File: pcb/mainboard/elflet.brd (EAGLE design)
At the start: 32 x 58 mm, 37 parts, among them J1 ZX62-B-5PA(33), J2 2212S-10SG-36, J3 STD-PINHD-1X6, Q1 IRLML6344TRPBF, Q2 ALS-PT19-315C/L177/TR8, SW1 SKRPACE010, U1 ESP-WROOM-32, U2 ADP3338AKCZ-3.3, U3 OSRB38C9AA, U4 BME280

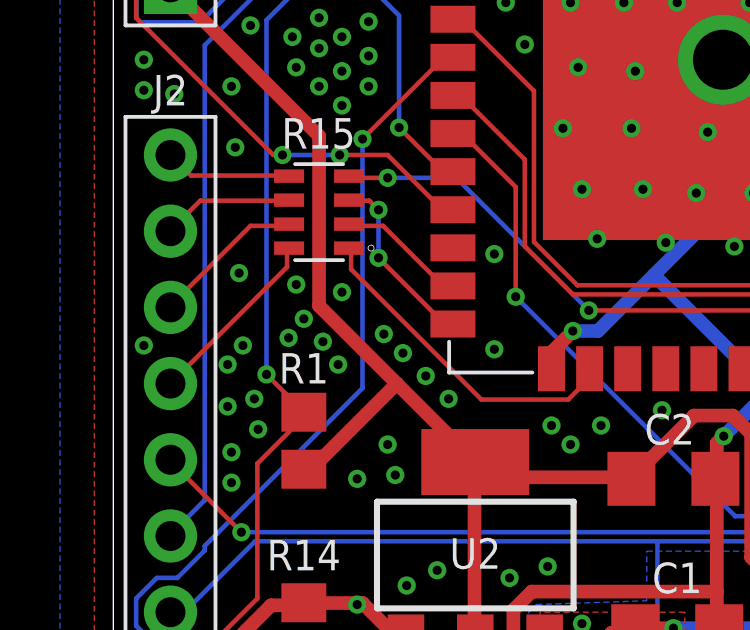
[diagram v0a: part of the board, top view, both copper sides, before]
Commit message: add logo silk
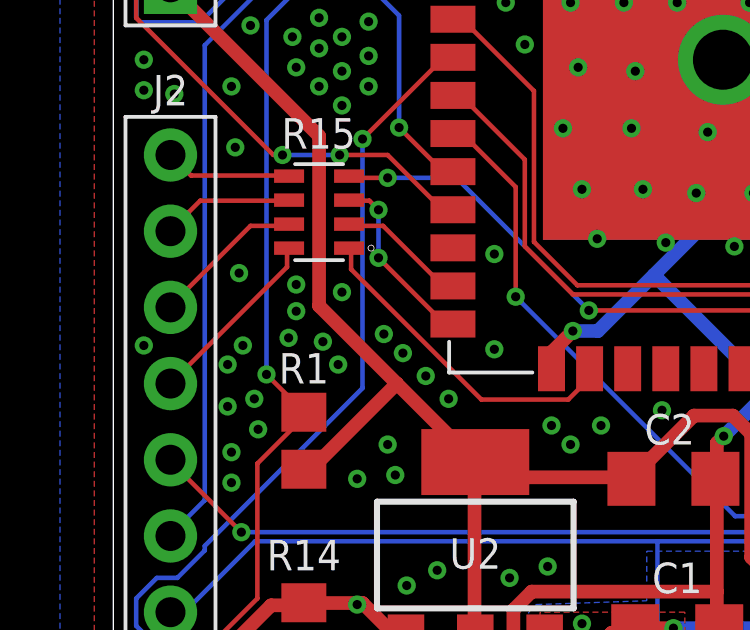
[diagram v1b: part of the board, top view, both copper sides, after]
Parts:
- added U$1: (no value), logo:ELFLET-LOGO
- added U$2: (no value), logo:ELFLET-QRCODE
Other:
- board text added: "ver 1.0"
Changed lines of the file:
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@@
 <dimension x1="0" y1="58" x2="32" y2="58" x3="16" y3="64.77" textsize="1.778" layer="47" visible="yes"/>
 <dimension x1="0" y1="0" x2="0" y2="58" x3="-8.89" y3="29" textsize="1.778" layer="47" visible="yes"/>
+<text x="12.319" y="5.588" size="1.4224" layer="22" font="vector" rot="MR0">ver 1.0</text>
 </plain>
 <attributes>
@@
 <attribute name="VALUE" x="-0.592" y="54.862" size="1.27" layer="27" font="vector" rot="R270" align="center"/>
 </element>
+<element name="U$1" library="logo" package="ELFLET-LOGO" value="" x="26.924" y="7.747" rot="MR0"/>
+<element name="U$2" library="logo" package="ELFLET-QRCODE" value="" x="25.908" y="33.528" rot="MR0"/>
 </elements>
 <signals>
@@
 <via x="7.493" y="17.78" extent="1-16" drill="0.3048"/>
 <via x="6.985" y="18.542" extent="1-16" drill="0.3048"/>
-<via x="6.35" y="19.304" extent="1-16" drill="0.3048"/>
+<via x="6.096" y="19.558" extent="1-16" drill="0.3048"/>
 <via x="6.096" y="20.447" extent="1-16" drill="0.3048"/>
 <via x="5.842" y="18.669" extent="1-16" drill="0.3048"/>

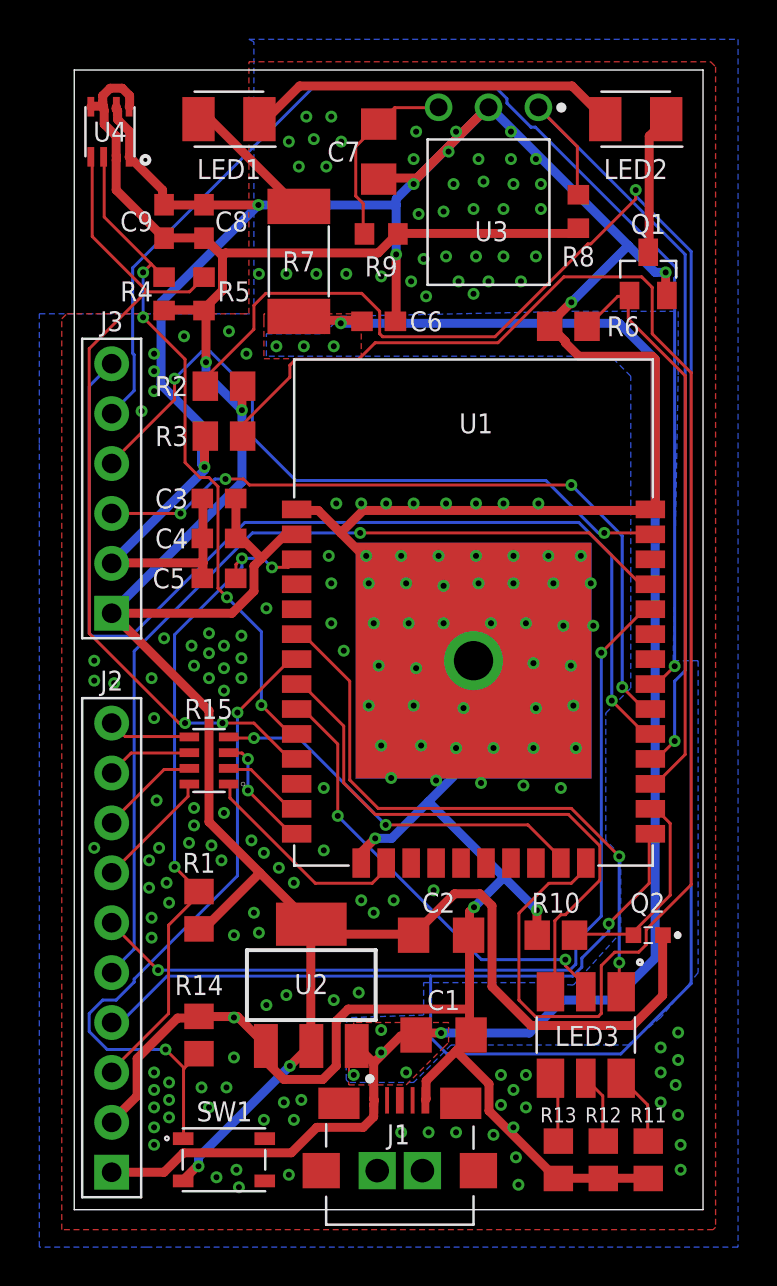
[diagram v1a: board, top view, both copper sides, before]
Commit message: optimized for panerizing
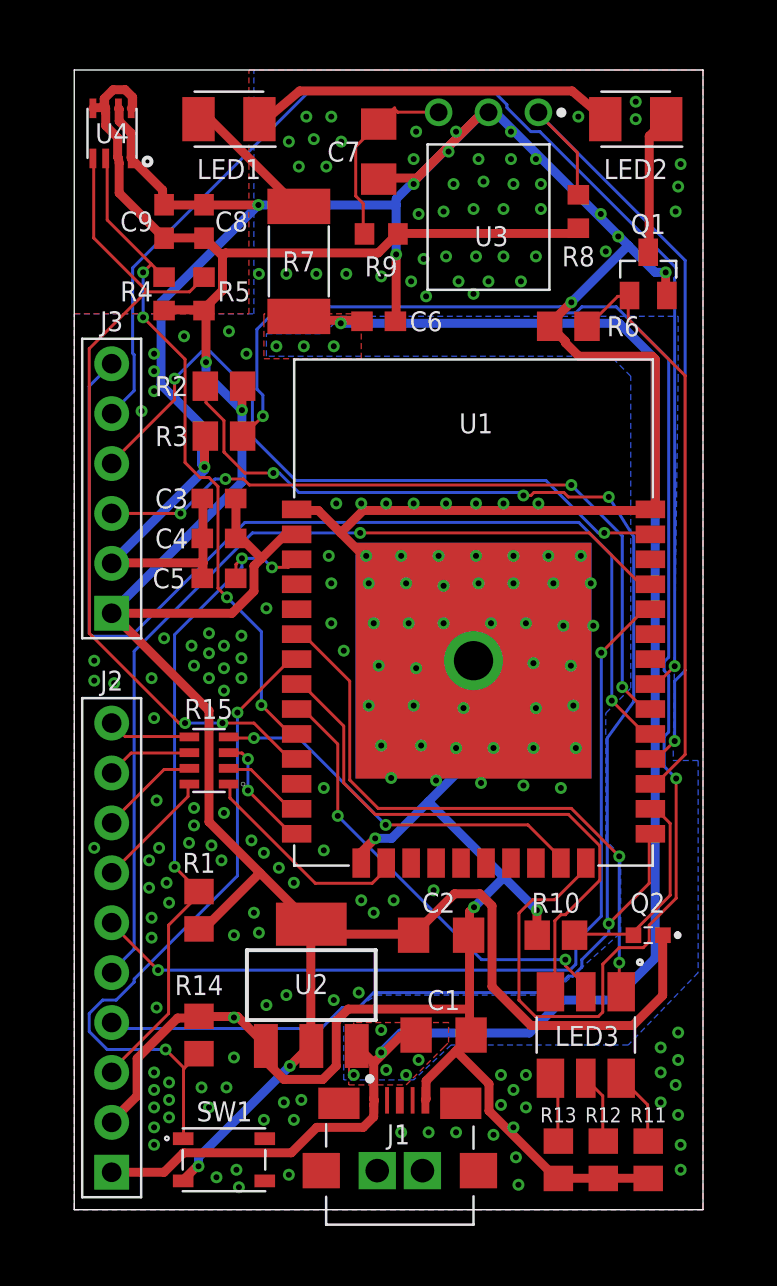
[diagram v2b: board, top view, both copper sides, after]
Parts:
- moved U3 0.25 mm to (21.1, 54.8)
- moved U4 0.13 mm to (2.90, 55.8)
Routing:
- net BOOT: track 122.9 -> 80.6 mm, vias 2 -> 4
- net +5V: track 85.8 -> 88.1 mm, vias 9 -> 10
- net N$5: track 9.70 -> 10.9 mm
- net N$1: track 79.2 -> 78.6 mm, vias 0 -> 2
- net IRRX: track 42.5 -> 42.0 mm
- net GND: track 207.9 -> 208.0 mm, vias 201 -> 211
